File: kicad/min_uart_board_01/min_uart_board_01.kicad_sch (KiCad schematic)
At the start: 13 parts, among them J1 DIN41612_02x32_AC, J2 UART1, J3 UART2, U10 TL28L92FR, U13 74AHC1G32, Y1 Crystal 3.6864MHz

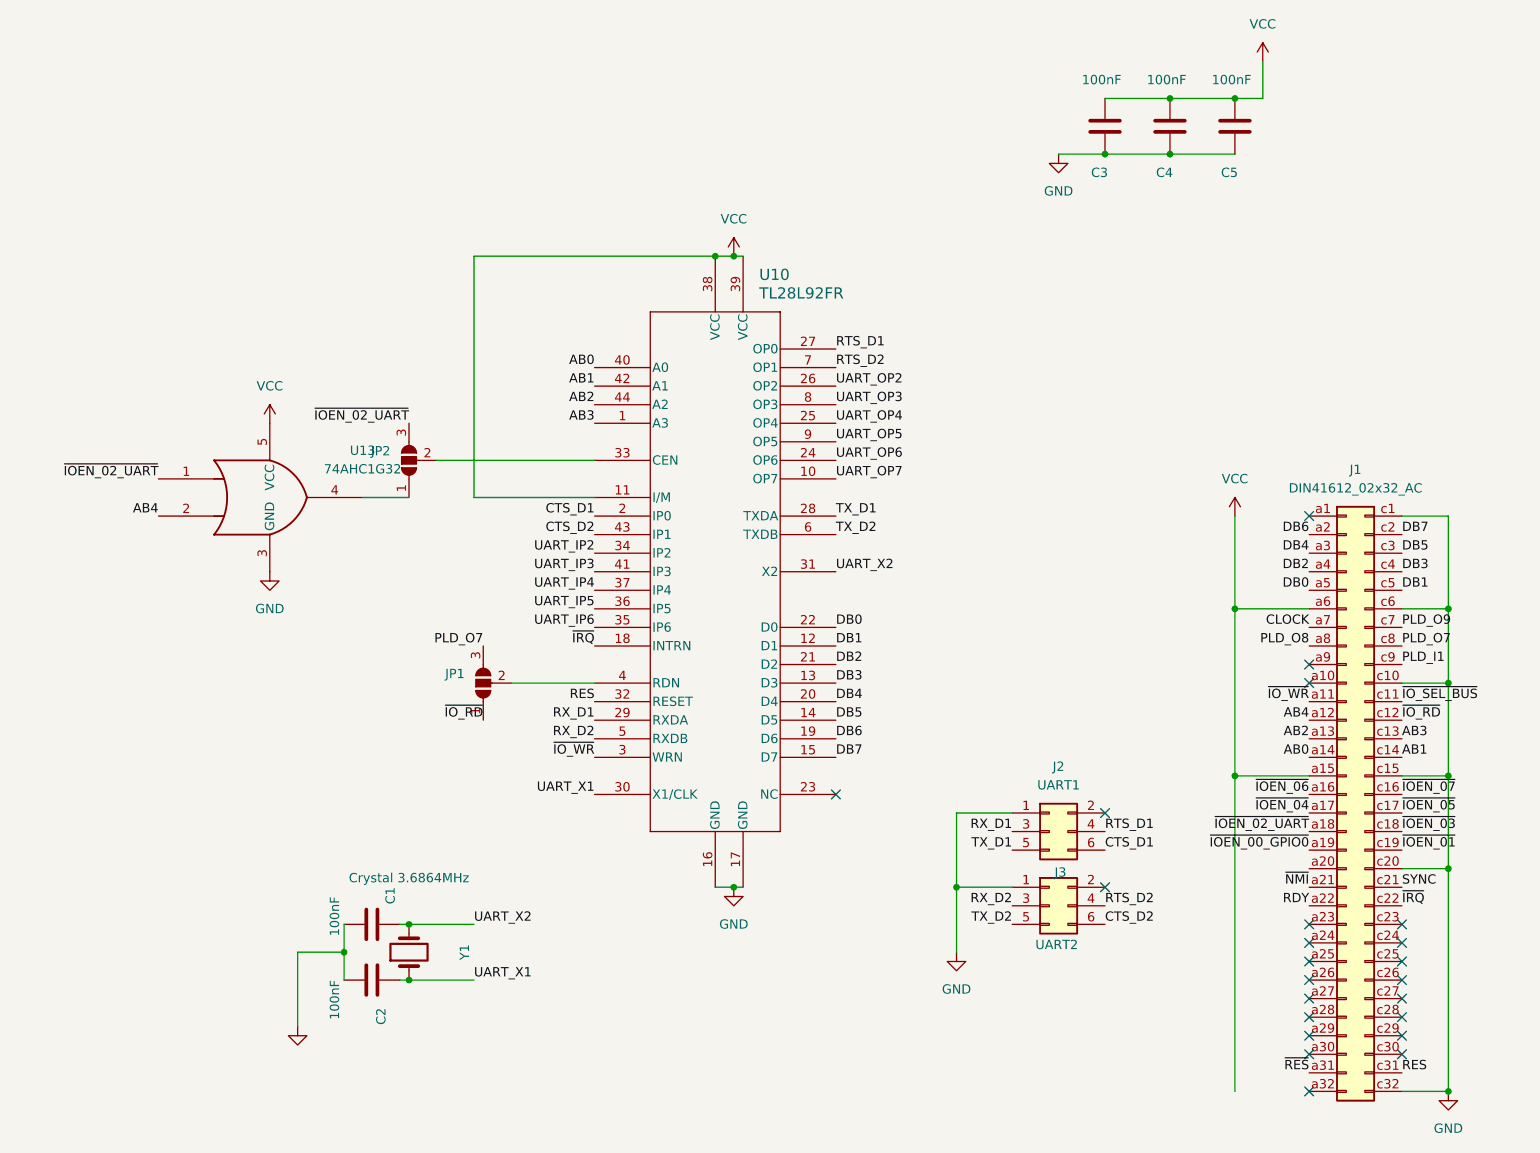
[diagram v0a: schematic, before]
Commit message: restoring min uart board from backup... some horrible mess happened
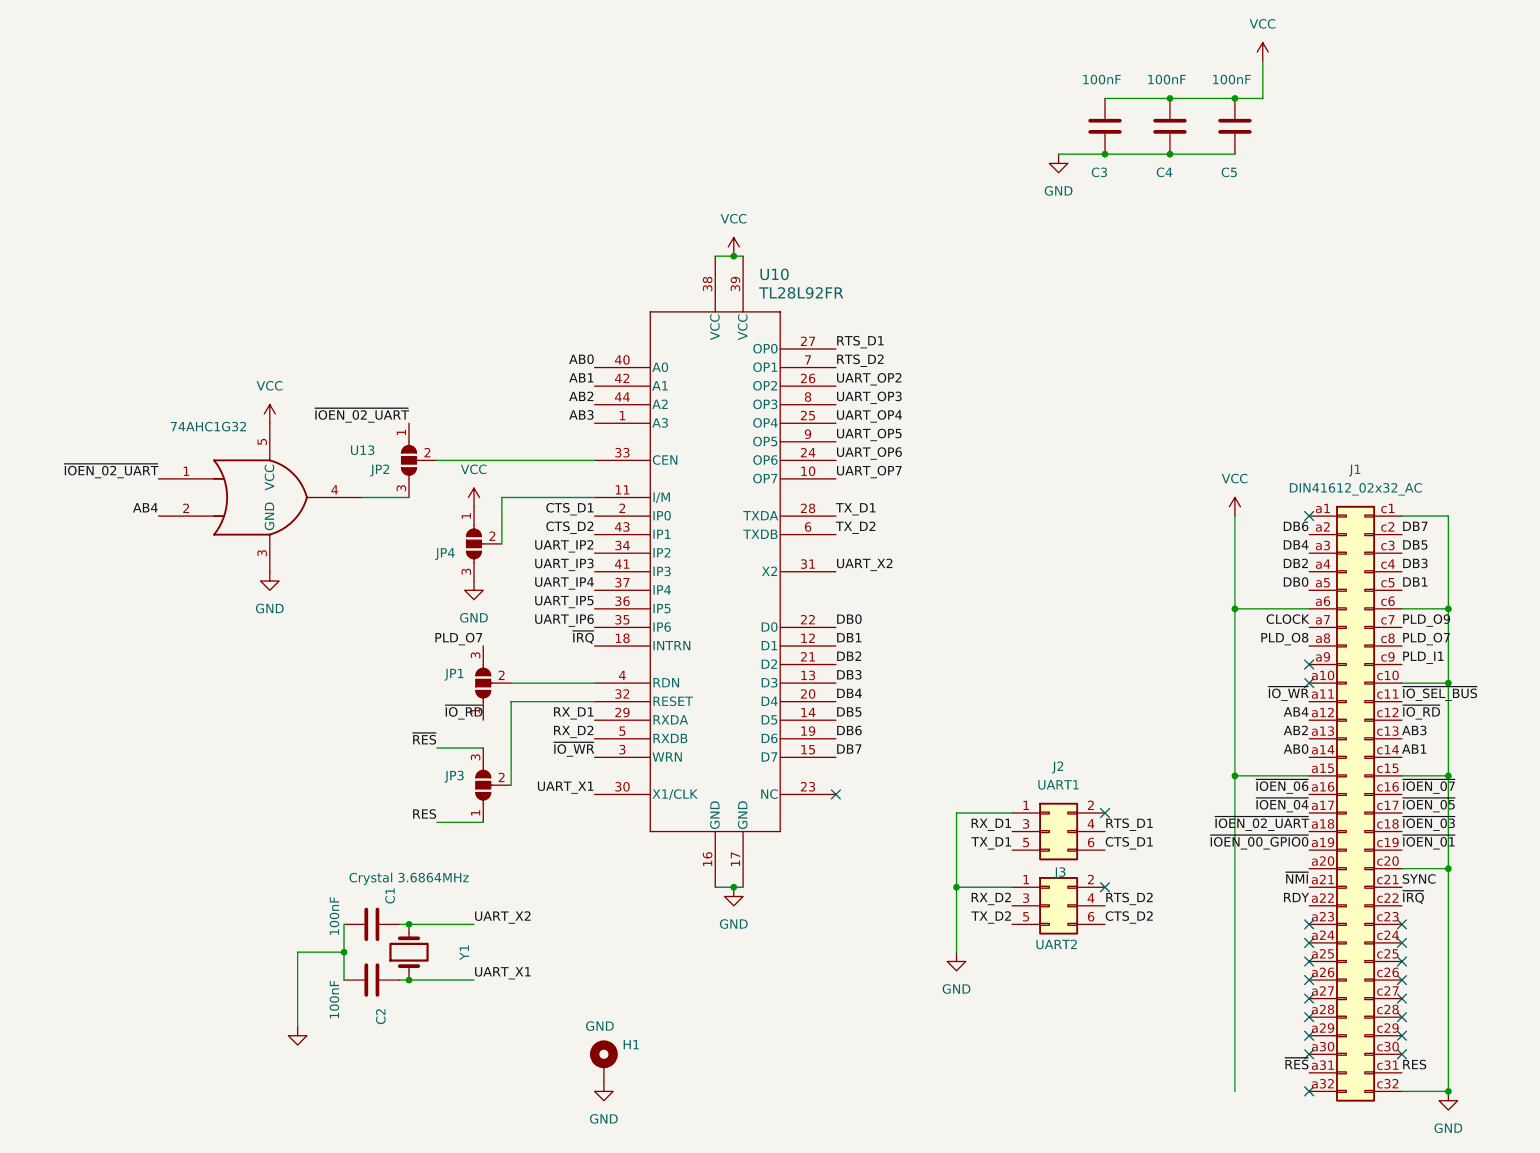
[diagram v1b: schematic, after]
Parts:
- added H1: GND, MountingHole:MountingHole_3.2mm_M3_DIN965_Pad, symbol Mechanical:MountingHole_Pad
- added JP3, JP4: SolderJumper_3_Open, Jumper:SolderJumper-3_P1.3mm_Open_RoundedPad1.0x1.5mm, symbol Jumper:SolderJumper_3_Open
- JP1, JP2: footprint Jumper:SolderJumper-3_P1.3mm_Open_RoundedPad1.0x1.5mm_NumberLabels -> Jumper:SolderJumper-3_P1.3mm_Open_RoundedPad1.0x1.5mm
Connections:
- net GND: now also H1.1, JP4.3 (B)
- net RES: now also JP3.1 (A); no longer U10.32 (RESET)
- net VCC: now also JP4.1 (A); no longer U10.11 (I/M)
- net ~{IOEN_02_UART}: now also JP2.1 (A); no longer JP2.3 (B)
- net ~{RES}: now also JP3.3 (B)
- net at U13.4: now also JP2.3 (B); no longer JP2.1 (A)
- new net: JP3.2 (C), U10.32 (RESET)
- new net: JP4.2 (C), U10.11 (I/M)
